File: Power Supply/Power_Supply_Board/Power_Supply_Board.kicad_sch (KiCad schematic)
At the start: 26 parts, among them SW1 Standby

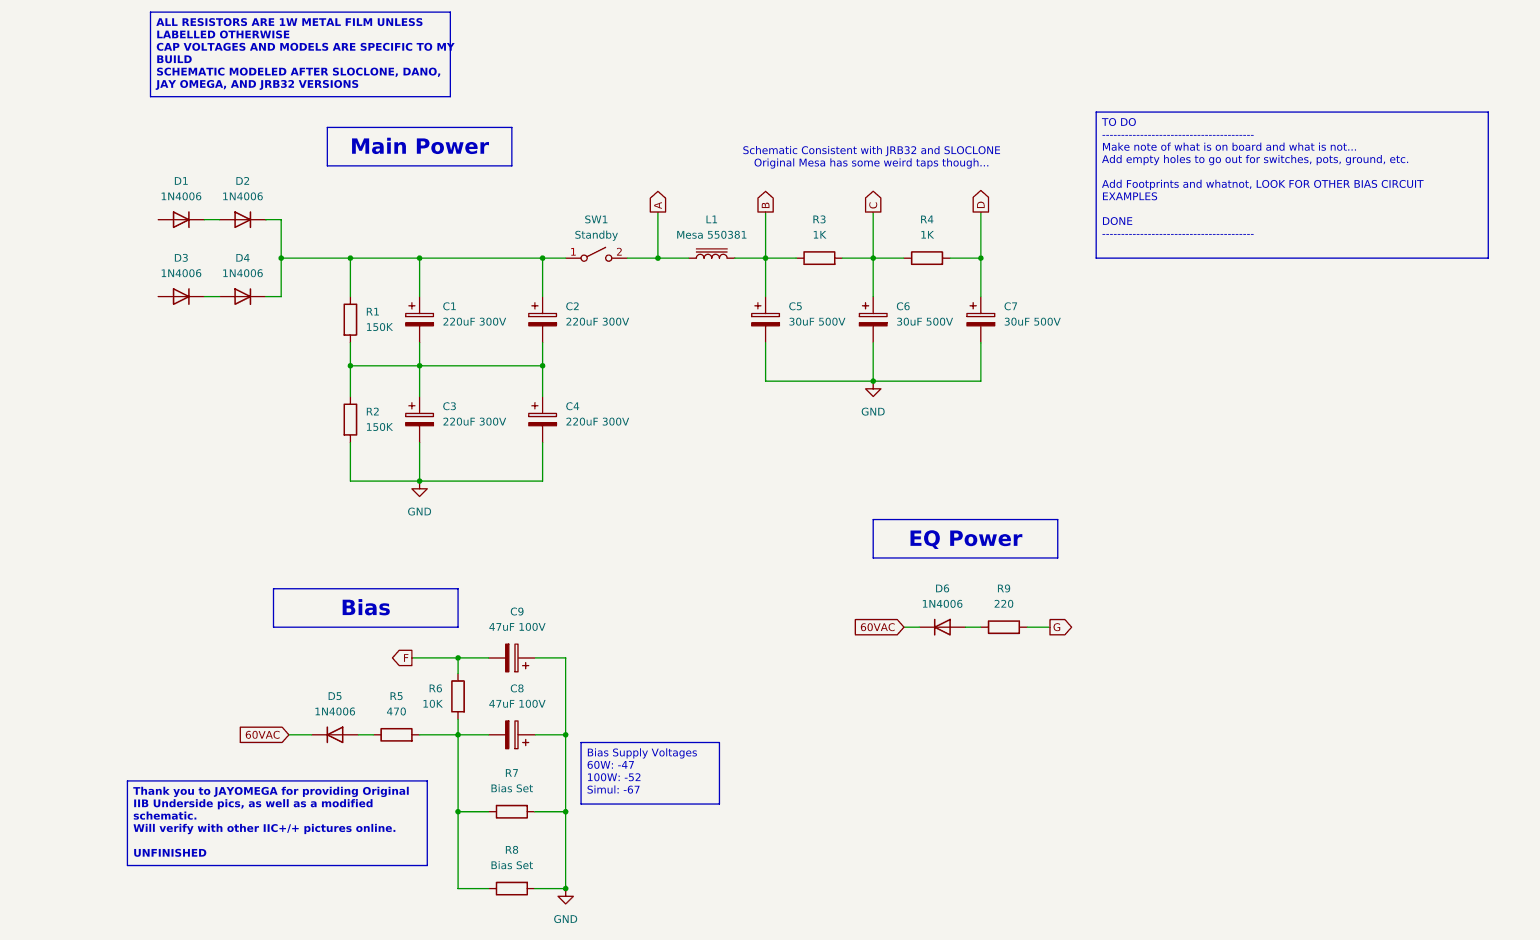
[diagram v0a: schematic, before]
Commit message: Started Power Supply Board, Made EQ Driver Changes
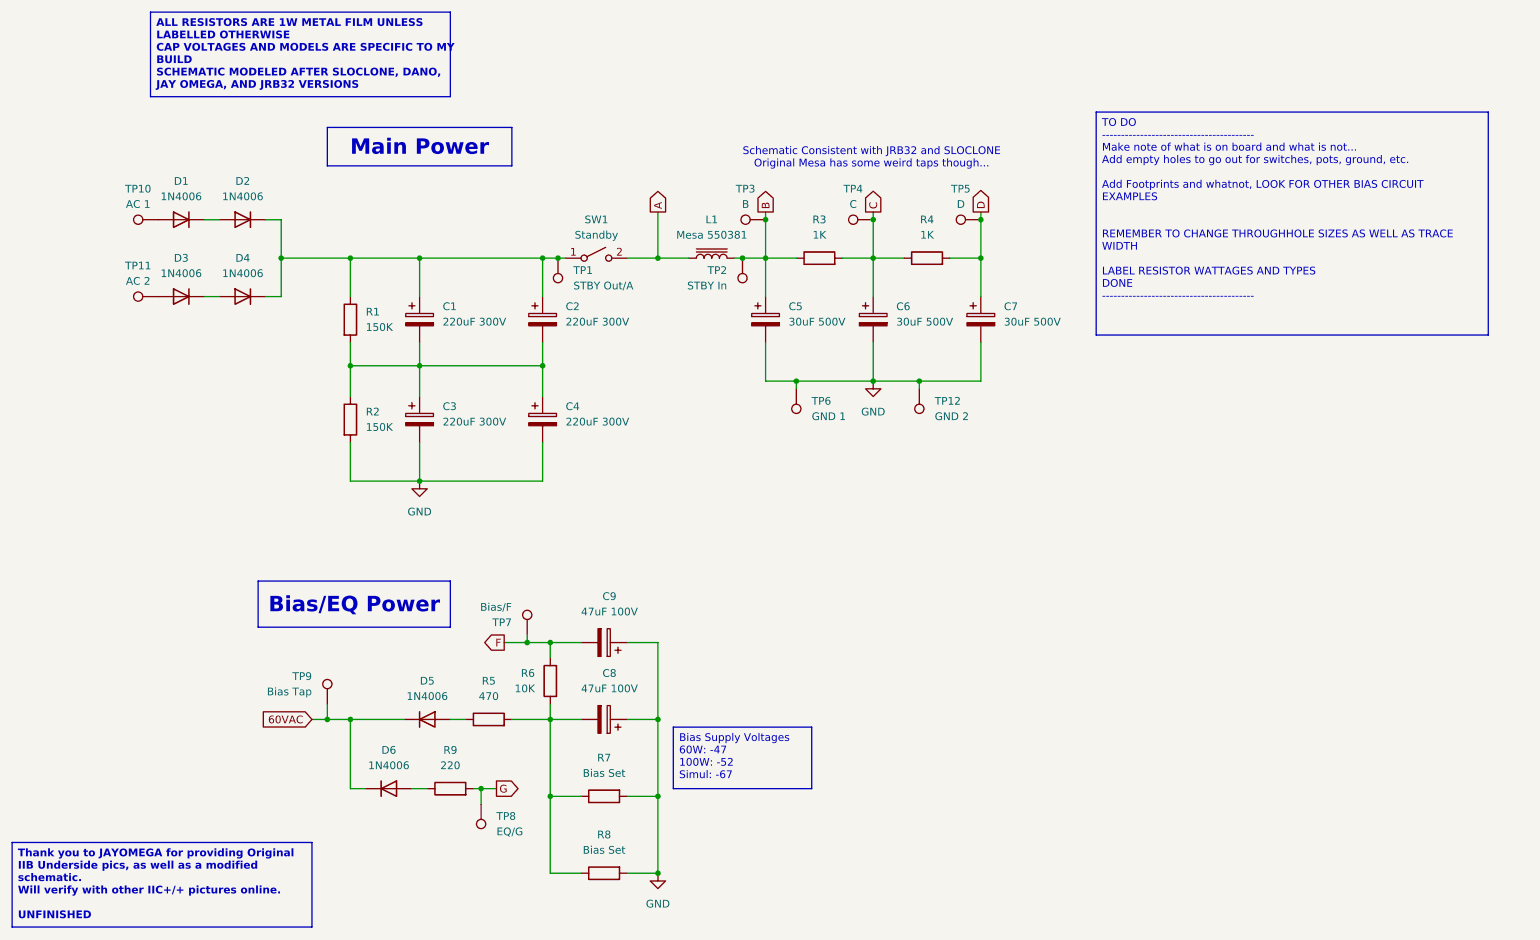
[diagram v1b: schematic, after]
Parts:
- added TP1: STBY Out/A, HiroFootprints:Out_Hole_3.4_1.8, symbol Connector:TestPoint
- added TP10: AC 1, HiroFootprints:Out_Hole_3.4_1.8, symbol Connector:TestPoint
- added TP11: AC 2, HiroFootprints:Out_Hole_3.4_1.8, symbol Connector:TestPoint
- added TP12: GND 2, HiroFootprints:Out_Hole_3.4_1.8, symbol Connector:TestPoint
- added TP2: STBY In, HiroFootprints:Out_Hole_3.4_1.8, symbol Connector:TestPoint
- added TP3: B, HiroFootprints:Out_Hole_3.4_1.8, symbol Connector:TestPoint
- added TP4: C, HiroFootprints:Out_Hole_3.4_1.8, symbol Connector:TestPoint
- added TP5: D, HiroFootprints:Out_Hole_3.4_1.8, symbol Connector:TestPoint
- added TP6: GND 1, HiroFootprints:Out_Hole_3.4_1.8, symbol Connector:TestPoint
- added TP7: Bias/F, HiroFootprints:Out_Hole_3.4_1.8, symbol Connector:TestPoint
- added TP8: EQ/G, HiroFootprints:Out_Hole_3.4_1.8, symbol Connector:TestPoint
- added TP9: Bias Tap, HiroFootprints:Out_Hole_3.4_1.8, symbol Connector:TestPoint
- C1, C2, C3, C4: footprint (none) -> Capacitor_THT:CP_Axial_L30.0mm_D18.0mm_P35.00mm_Horizontal
- C5, C6, C7: footprint (none) -> Capacitor_THT:CP_Axial_L38.0mm_D21.0mm_P44.00mm_Horizontal
- C8, C9: footprint (none) -> Capacitor_THT:CP_Axial_L18.0mm_D8.0mm_P25.00mm_Horizontal
- R1, R2, R3, R4, R5, R9: footprint (none) -> Resistor_THT:R_Axial_DIN0516_L15.5mm_D5.0mm_P20.32mm_Horizontal
- R6, R7, R8: footprint (none) -> Resistor_THT:R_Axial_DIN0411_L9.9mm_D3.6mm_P15.24mm_Horizontal
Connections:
- net 60VAC: now also TP9.1
- net B: now also TP2.1, TP3.1
- net C: now also TP4.1
- net D: now also TP5.1
- net F: now also TP7.1
- net G: now also TP8.1
- net GND: now also TP12.1, TP6.1
- net at C1.1, C2.1, D2.1 (K)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: now also TP1.1
- net at D1.2 (A): now also TP10.1
- net at D3.2 (A): now also TP11.1
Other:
- moved on the sheet: C8, C9, D5, D6, R5, R6, R7, R8, R9

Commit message: Power Supply Board Progress
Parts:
- C1, C2, C3, C4: footprint Capacitor_THT:CP_Axial_L30.0mm_D18.0mm_P35.00mm_Horizontal -> Capacitor_THT:CP_Axial_L55.0mm_D26.0mm_P60.00mm_Horizontal
- C5, C6, C7: footprint Capacitor_THT:CP_Axial_L38.0mm_D21.0mm_P44.00mm_Horizontal -> Capacitor_THT:CP_Axial_L42.0mm_D26.0mm_P45.00mm_Horizontal
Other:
- moved on the sheet: D5, R5
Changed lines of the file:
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@@
 	(wire
 		(pts
-			(xy 90.17 152.4) (xy 99.06 152.4)
+			(xy 90.17 152.4) (xy 92.71 152.4)
 		)
 		(stroke
@@
 	(wire
 		(pts
-			(xy 109.22 152.4) (xy 106.68 152.4)
+			(xy 102.87 152.4) (xy 100.33 152.4)
 		)
 		(stroke
@@
 	(wire
 		(pts
-			(xy 116.84 152.4) (xy 123.19 152.4)
+			(xy 110.49 152.4) (xy 123.19 152.4)
 		)
 		(stroke
@@
 			)
 		)
-		(property "Footprint" "Capacitor_THT:CP_Axial_L38.0mm_D21.0mm_P44.00mm_Horizontal"
+		(property "Footprint" "Capacitor_THT:CP_Axial_L42.0mm_D26.0mm_P45.00mm_Horizontal"
 			(at 159.7152 90.17 0)
 			(effects
@@
 			)
 		)
-		(property "Footprint" "Capacitor_THT:CP_Axial_L30.0mm_D18.0mm_P35.00mm_Horizontal"
+		(property "Footprint" "Capacitor_THT:CP_Axial_L55.0mm_D26.0mm_P60.00mm_Horizontal"
 			(at 102.5652 106.68 0)
 			(effects
@@
 			)
 		)
-		(property "Footprint" "Capacitor_THT:CP_Axial_L30.0mm_D18.0mm_P35.00mm_Horizontal"
+		(property "Footprint" "Capacitor_THT:CP_Axial_L55.0mm_D26.0mm_P60.00mm_Horizontal"
 			(at 102.5652 90.17 0)
 			(effects
@@
 			)
 		)
-		(property "Footprint" "Capacitor_THT:CP_Axial_L38.0mm_D21.0mm_P44.00mm_Horizontal"
+		(property "Footprint" "Capacitor_THT:CP_Axial_L42.0mm_D26.0mm_P45.00mm_Horizontal"
 			(at 195.2752 90.17 0)
 			(effects
@@
 	(symbol
 		(lib_id "Diode:1N4006")
-		(at 102.87 152.4 0)
+		(at 96.52 152.4 0)
 		(unit 1)
 		(exclude_from_sim no)
@@
 		(dnp no)
 		(property "Reference" "D5"
-			(at 102.87 146.05 0)
+			(at 96.52 146.05 0)
 			(effects
 				(font
@@
 		)
 		(property "Value" "1N4006"
-			(at 102.87 148.59 0)
+			(at 96.52 148.59 0)
 			(effects
 				(font
@@
 		)
 		(property "Footprint" "Diode_THT:D_DO-41_SOD81_P10.16mm_Horizontal"
-			(at 102.87 156.845 0)
+			(at 96.52 156.845 0)
 			(effects
 				(font
@@
 		)
 		(property "Datasheet" "http://www.vishay.com/docs/88503/1n4001.pdf"
-			(at 102.87 152.4 0)
+			(at 96.52 152.4 0)
 			(effects
 				(font
@@
 		)
 		(property "Description" "800V 1A General Purpose Rectifier Diode, DO-41"
-			(at 102.87 152.4 0)
+			(at 96.52 152.4 0)
 			(effects
 				(font
@@
 		)
 		(property "Sim.Device" "D"
-			(at 102.87 152.4 0)
+			(at 96.52 152.4 0)
 			(effects
 				(font
@@
 		)
 		(property "Sim.Pins" "1=K 2=A"
-			(at 102.87 152.4 0)
+			(at 96.52 152.4 0)
 			(effects
 				(font
@@
 			)
 		)
-		(property "Footprint" "Capacitor_THT:CP_Axial_L38.0mm_D21.0mm_P44.00mm_Horizontal"
+		(property "Footprint" "Capacitor_THT:CP_Axial_L42.0mm_D26.0mm_P45.00mm_Horizontal"
 			(at 177.4952 90.17 0)
 			(effects
@@
 			)
 		)
-		(property "Footprint" "Capacitor_THT:CP_Axial_L30.0mm_D18.0mm_P35.00mm_Horizontal"
+		(property "Footprint" "Capacitor_THT:CP_Axial_L55.0mm_D26.0mm_P60.00mm_Horizontal"
 			(at 122.8852 90.17 0)
 			(effects
@@
 			)
 		)
-		(property "Footprint" "Capacitor_THT:CP_Axial_L30.0mm_D18.0mm_P35.00mm_Horizontal"
+		(property "Footprint" "Capacitor_THT:CP_Axial_L55.0mm_D26.0mm_P60.00mm_Horizontal"
 			(at 122.8852 106.68 0)
 			(effects
@@
 	(symbol
 		(lib_id "Device:R")
-		(at 113.03 152.4 90)
+		(at 106.68 152.4 90)
 		(unit 1)
 		(exclude_from_sim no)
@@
 		(fields_autoplaced yes)
 		(property "Reference" "R5"
-			(at 113.03 146.05 90)
+			(at 106.68 146.05 90)
 			(effects
 				(font
@@
 		)
 		(property "Value" "470"
-			(at 113.03 148.59 90)
+			(at 106.68 148.59 90)
 			(effects
 				(font
@@
 		)
 		(property "Footprint" "Resistor_THT:R_Axial_DIN0516_L15.5mm_D5.0mm_P20.32mm_Horizontal"
-			(at 113.03 154.178 90)
+			(at 106.68 154.178 90)
 			(effects
 				(font
@@
 		)
 		(property "Datasheet" "~"
-			(at 113.03 152.4 0)
+			(at 106.68 152.4 0)
 			(effects
 				(font
@@
 		)
 		(property "Description" "Resistor"
-			(at 113.03 152.4 0)
+			(at 106.68 152.4 0)
 			(effects
 				(font
